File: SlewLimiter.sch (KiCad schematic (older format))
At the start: 65 parts

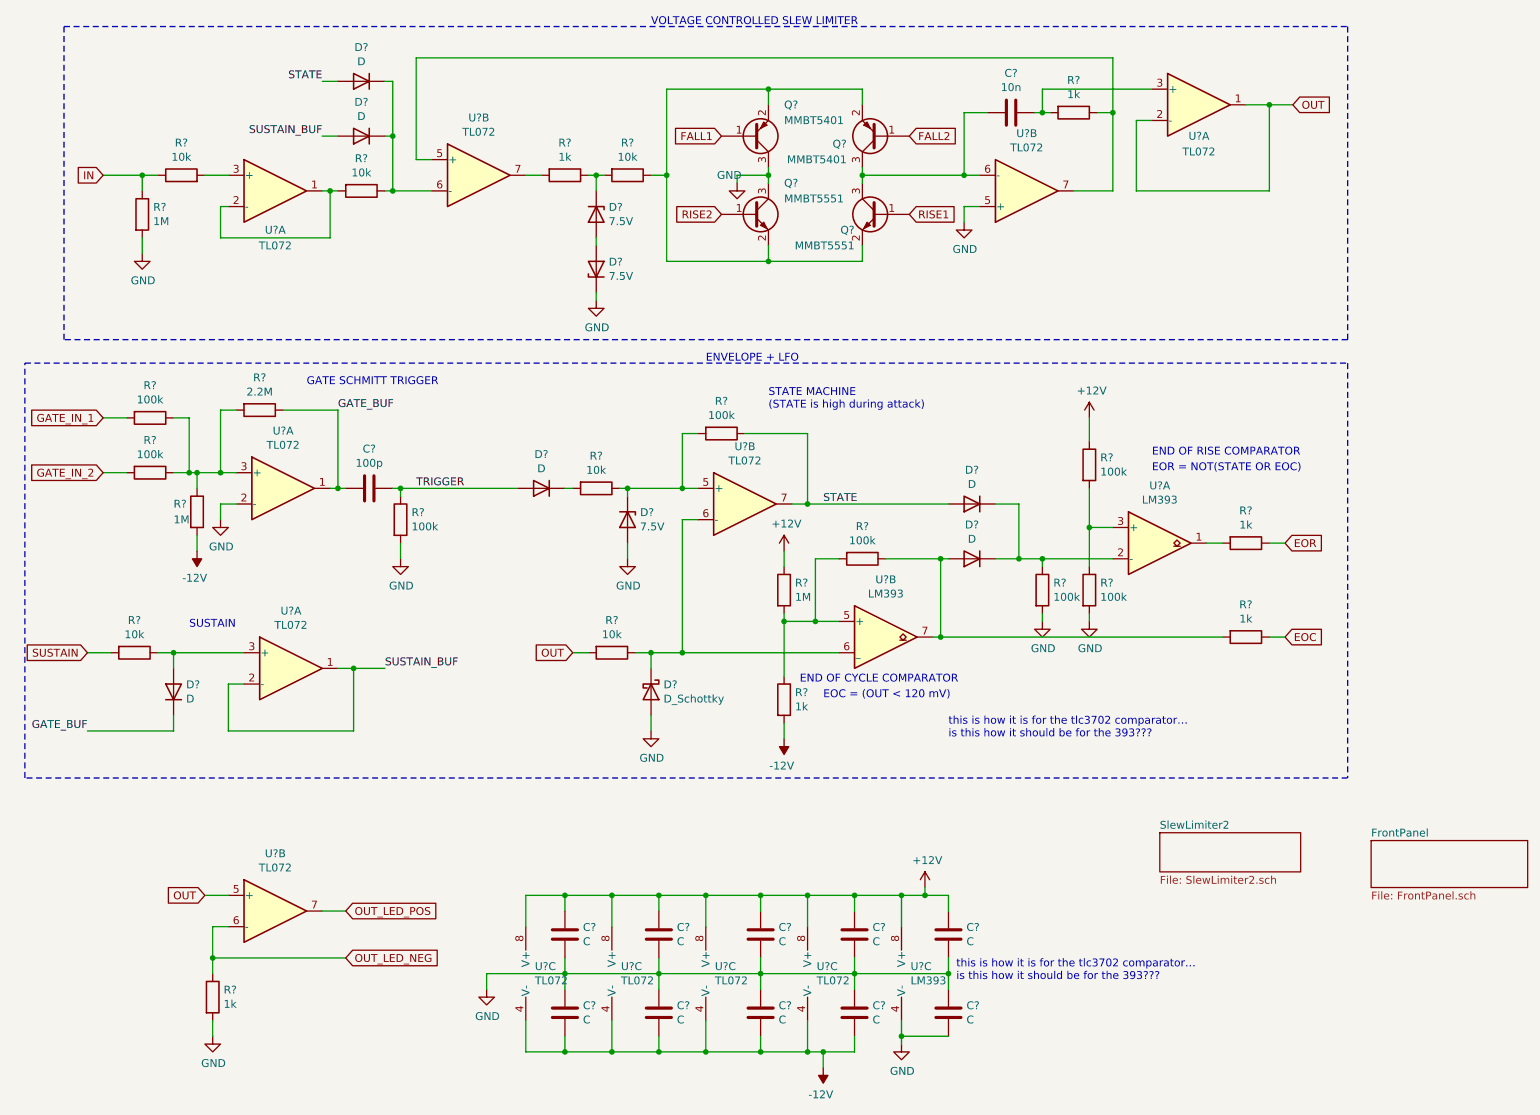
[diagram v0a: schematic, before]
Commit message: Labelled all component values
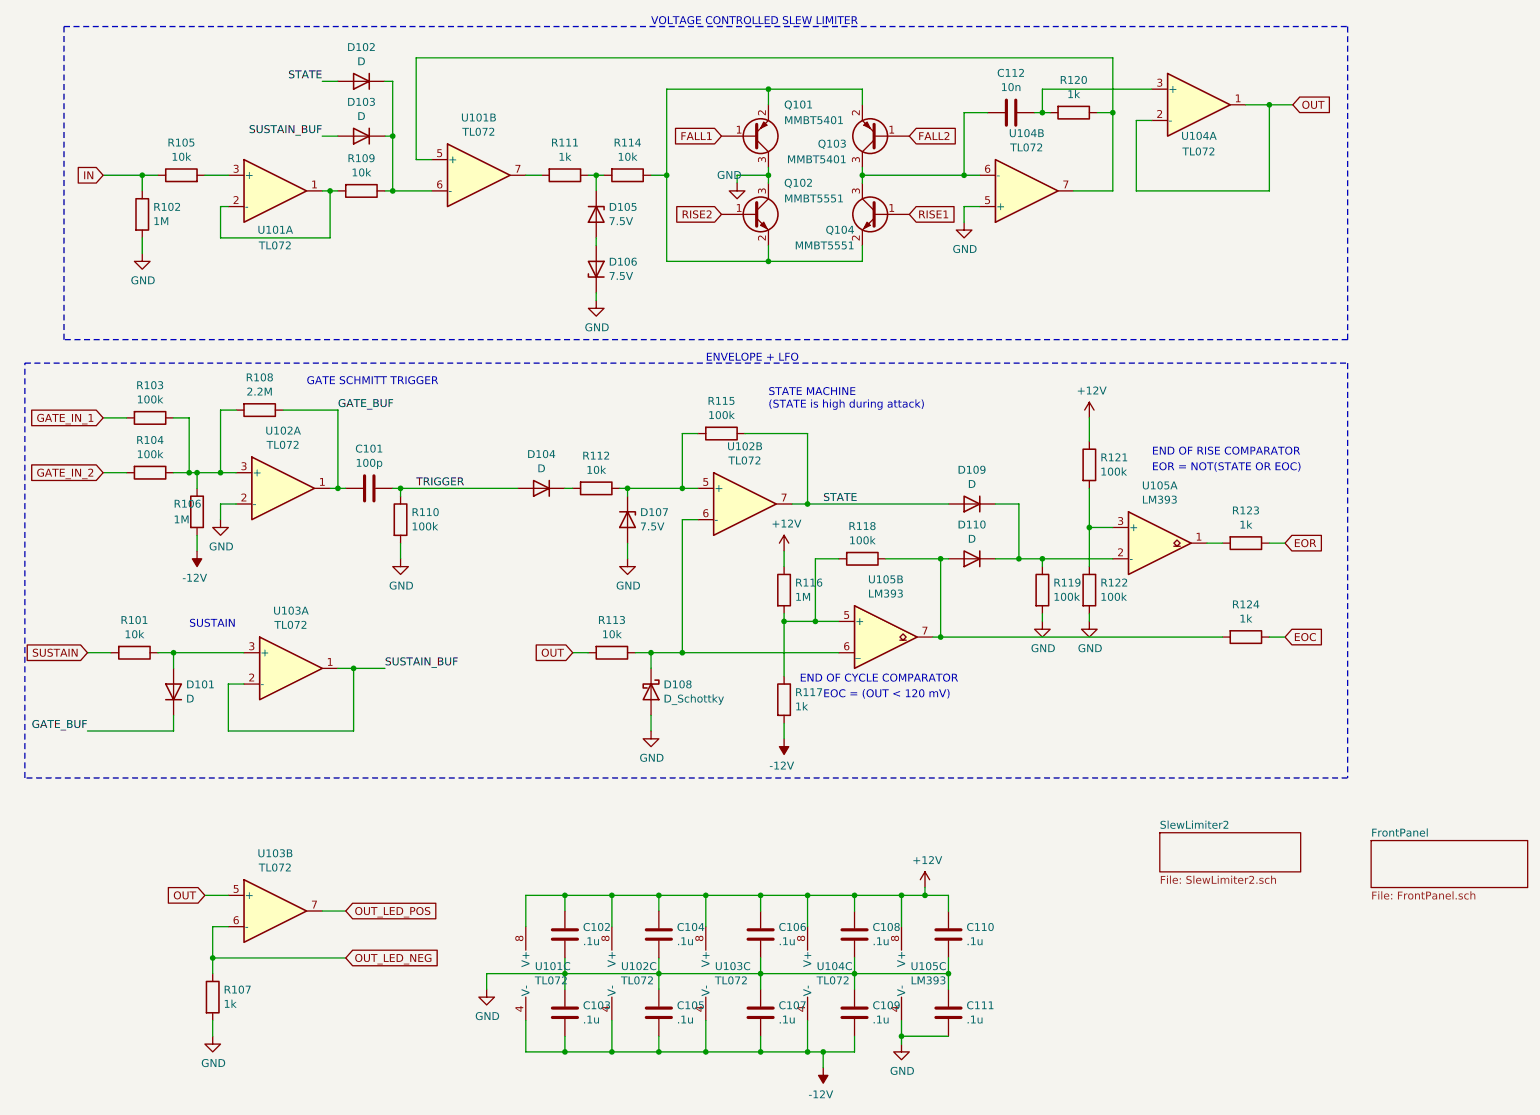
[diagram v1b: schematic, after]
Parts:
- C102, C103, C104, C105, C106, C107, C108, C109, C110, C111: renamed from C?; value C -> .1u
- gave numbers to parts that had none: 45
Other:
- note removed: "this is how it is for the tlc3702 comparator…\nis this how it should be for the 393???\n"
